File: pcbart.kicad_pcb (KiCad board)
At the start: 2 copper layers, 159.1 x 29.1 mm, 5 parts

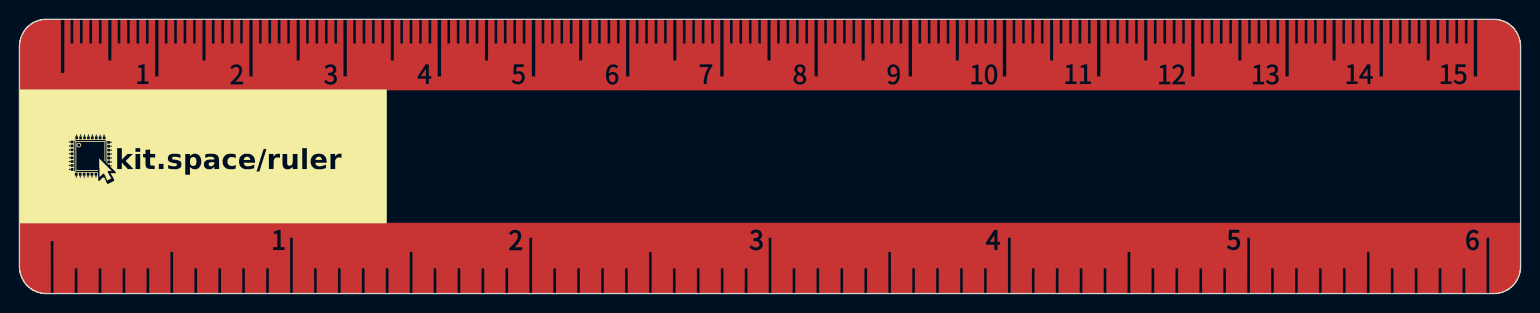
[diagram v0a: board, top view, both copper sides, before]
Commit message: More silkscreen, switch to svg2shenzhen dev vers.
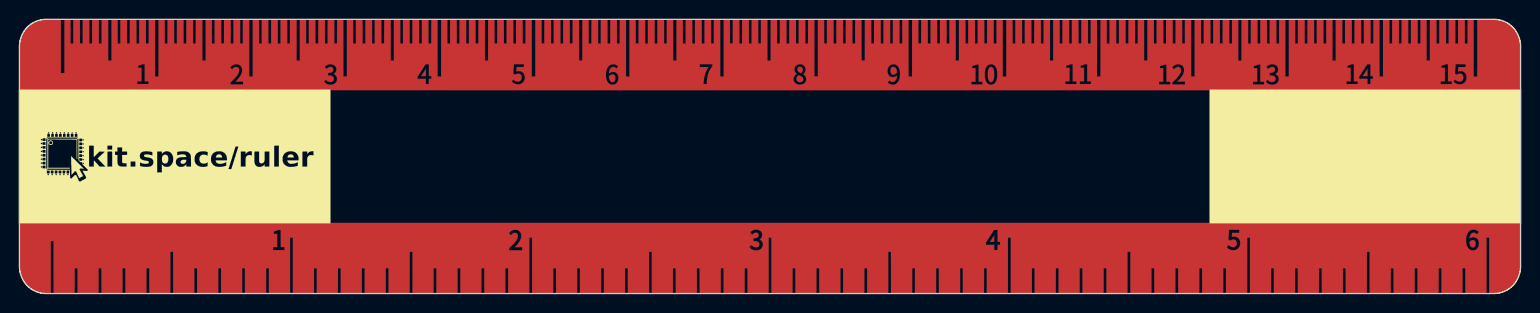
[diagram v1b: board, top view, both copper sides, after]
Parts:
- removed the G*** at (0.00, 0.00) (x5)
- added G*** (x6): LOGO, LOGO, F.Cu at (0.00, 0.00)
